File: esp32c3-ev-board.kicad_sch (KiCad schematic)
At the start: 33 parts, among them IC1 ESP32-C3, IC2 W25Q128JVSIQ, IC3 ACS711EEXTK-31AB-T, J1 Battery Neg(Series), J2 Battery Pos, SW1 SW_DPST_x2, Y1 40MHZ

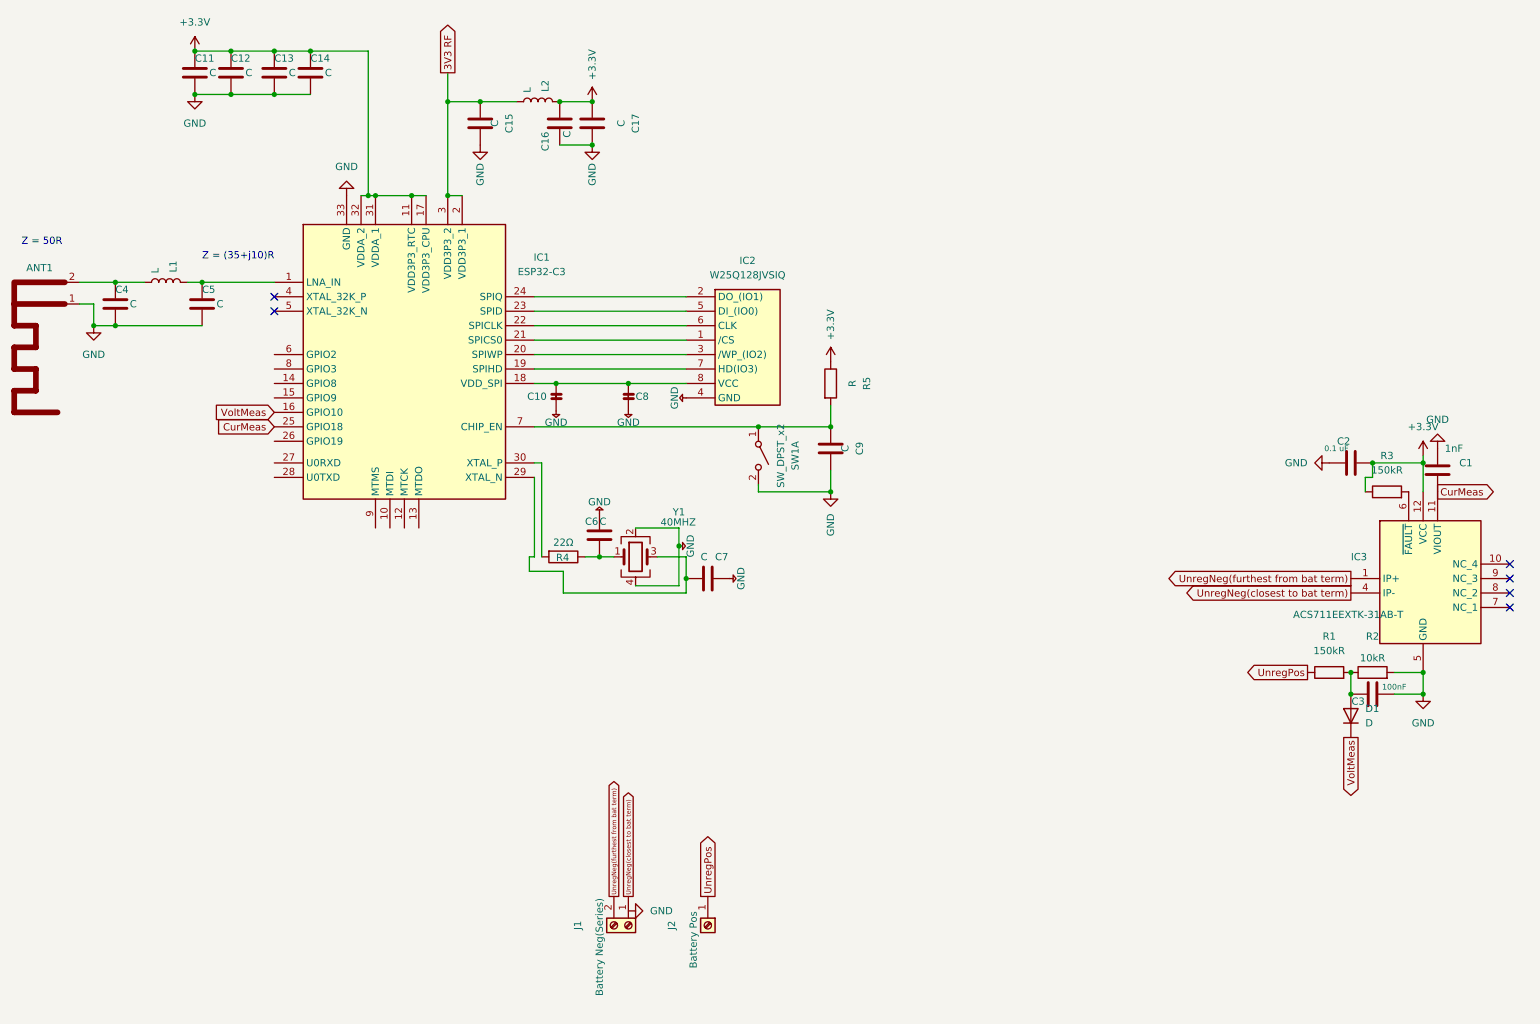
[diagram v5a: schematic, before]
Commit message: Tidy values and usb/esd prot
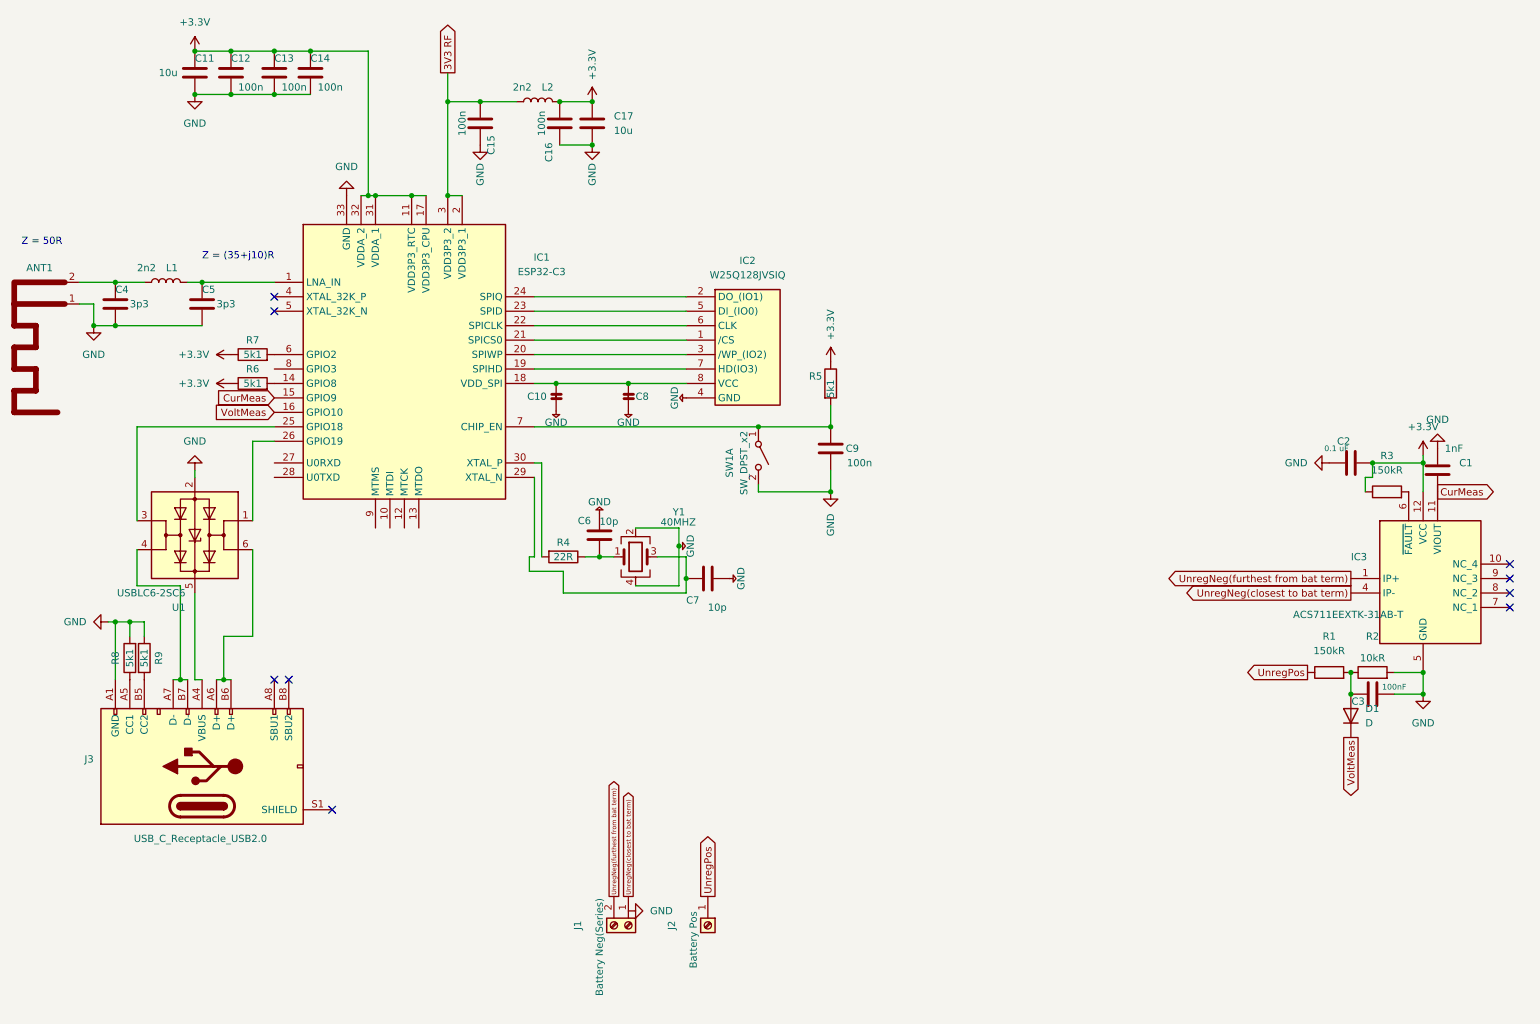
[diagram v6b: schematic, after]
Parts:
- added J3: USB_C_Receptacle_USB2.0, symbol Connector:USB_C_Receptacle_USB2.0
- added R6, R7, R8, R9: 5k1, symbol Device:R
- added U1: USBLC6-2SC6, Package_TO_SOT_SMD:SOT-23-6, symbol Power_Protection:USBLC6-2SC6
- C11, C17: value C -> 10u
- C12, C13, C14, C15, C16, C9: value C -> 100n
- C4, C5: value C -> 3p3
- C6, C7: value C -> 10p
- L1, L2: value L -> 2n2
- R4: value 22Ω -> 22R
- R5: value R -> 5k1
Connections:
- net +3.3V: now also R6.1, R7.1
- net CurMeas: now also IC1.15 (GPIO9); no longer IC1.25 (GPIO18)
- net GND: now also J3.A1 (GND), J3.A9 (VBUS), J3.B4 (VBUS), J3.B9 (VBUS), R8.2, R9.1, U1.2 (GND)
- net at IC1.14 (GPIO8): now also R6.2
- net at IC1.26 (GPIO19): now also U1.1 (I/O1)
- net at IC1.6 (GPIO2): now also R7.2
- new net: IC1.25 (GPIO18), U1.3 (I/O2)
- new net: J3.A7 (D-), J3.B7 (D-), U1.4 (I/O2)
- new net: J3.A4 (VBUS), U1.5 (VBUS)
- new net: J3.A6 (D+), J3.B6 (D+), U1.6 (I/O1)
- new net: J3.A5 (CC1), R8.1
- new net: J3.A12 (GND), J3.B1 (GND), J3.B12 (GND)
- new net: J3.B5 (CC2), R9.2
- no-connect marks 6 -> 9

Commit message: working on voltage and voltage mux
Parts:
- added C18: 100u, symbol Device:C_Polarized
- added C19: 1000u, symbol Device:C_Polarized
- added D2: MBR360, DIOAD2860W130L840D505, symbol MBR360:MBR360
- added L3: L, symbol Device:L
- added U2: LM2576HVS-3.3, Package_TO_SOT_SMD:TO-263-5_TabPin3, symbol Regulator_Switching:LM2576HVS-3.3
- IC1: value ESP32-C3 -> ESP32-C3FH4
- R1: value 150kR -> 180kR
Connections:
- net UnregNeg(closest to bat term) is gone; now on net GND: IC3.4 (IP-), J1.1 (Pin_1)
- net +3.3V: now also C19.1, L3.2, U2.4 (FB)
- net GND: now also C18.2, C19.2, D2.2 (A), U2.3 (GND), U2.5 (~{ON}/OFF)
- net UnregPos: now also C18.1, U2.1 (VIN)
- net VBUS: now reaches J3.A4 (VBUS), U1.5 (VBUS)
- new net: D2.1 (K), L3.1, U2.2 (OUT)
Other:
- note added: "If using external flash, use espfuse to burn EFUSE."
- note added: "MAX 60V"
- note added: "MAX 62.7V"
- moved on the sheet: U1

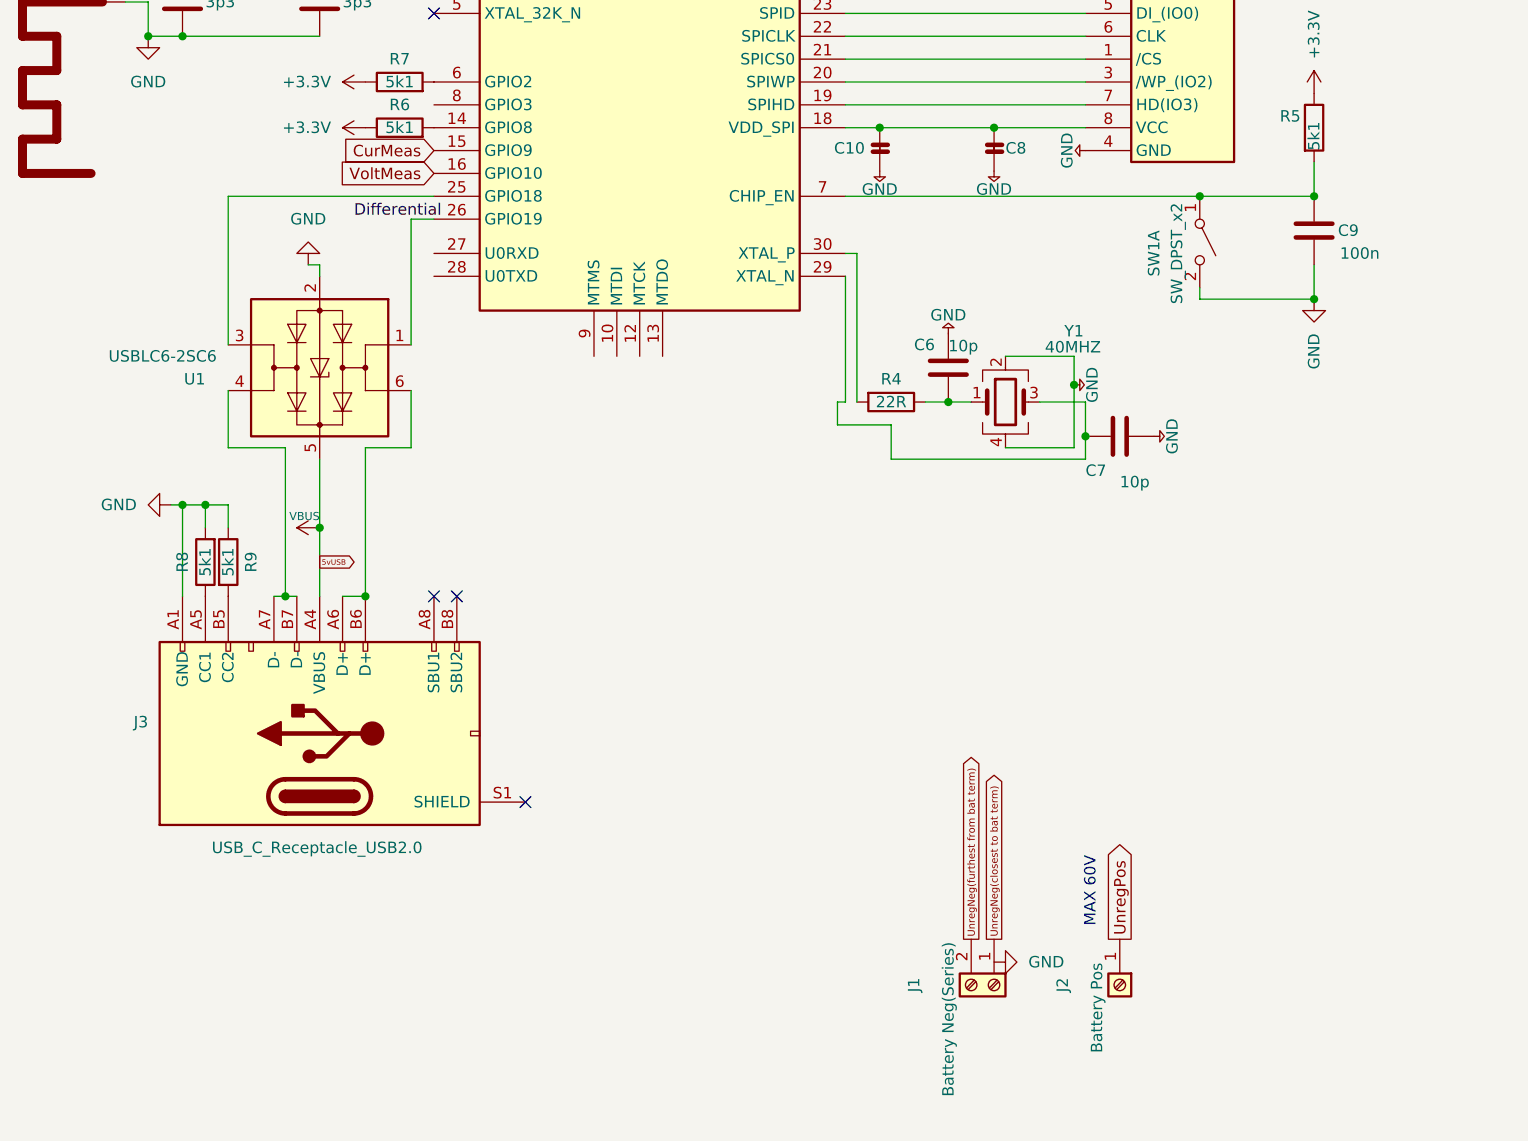
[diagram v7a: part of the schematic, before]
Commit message: Added Power supply diodes
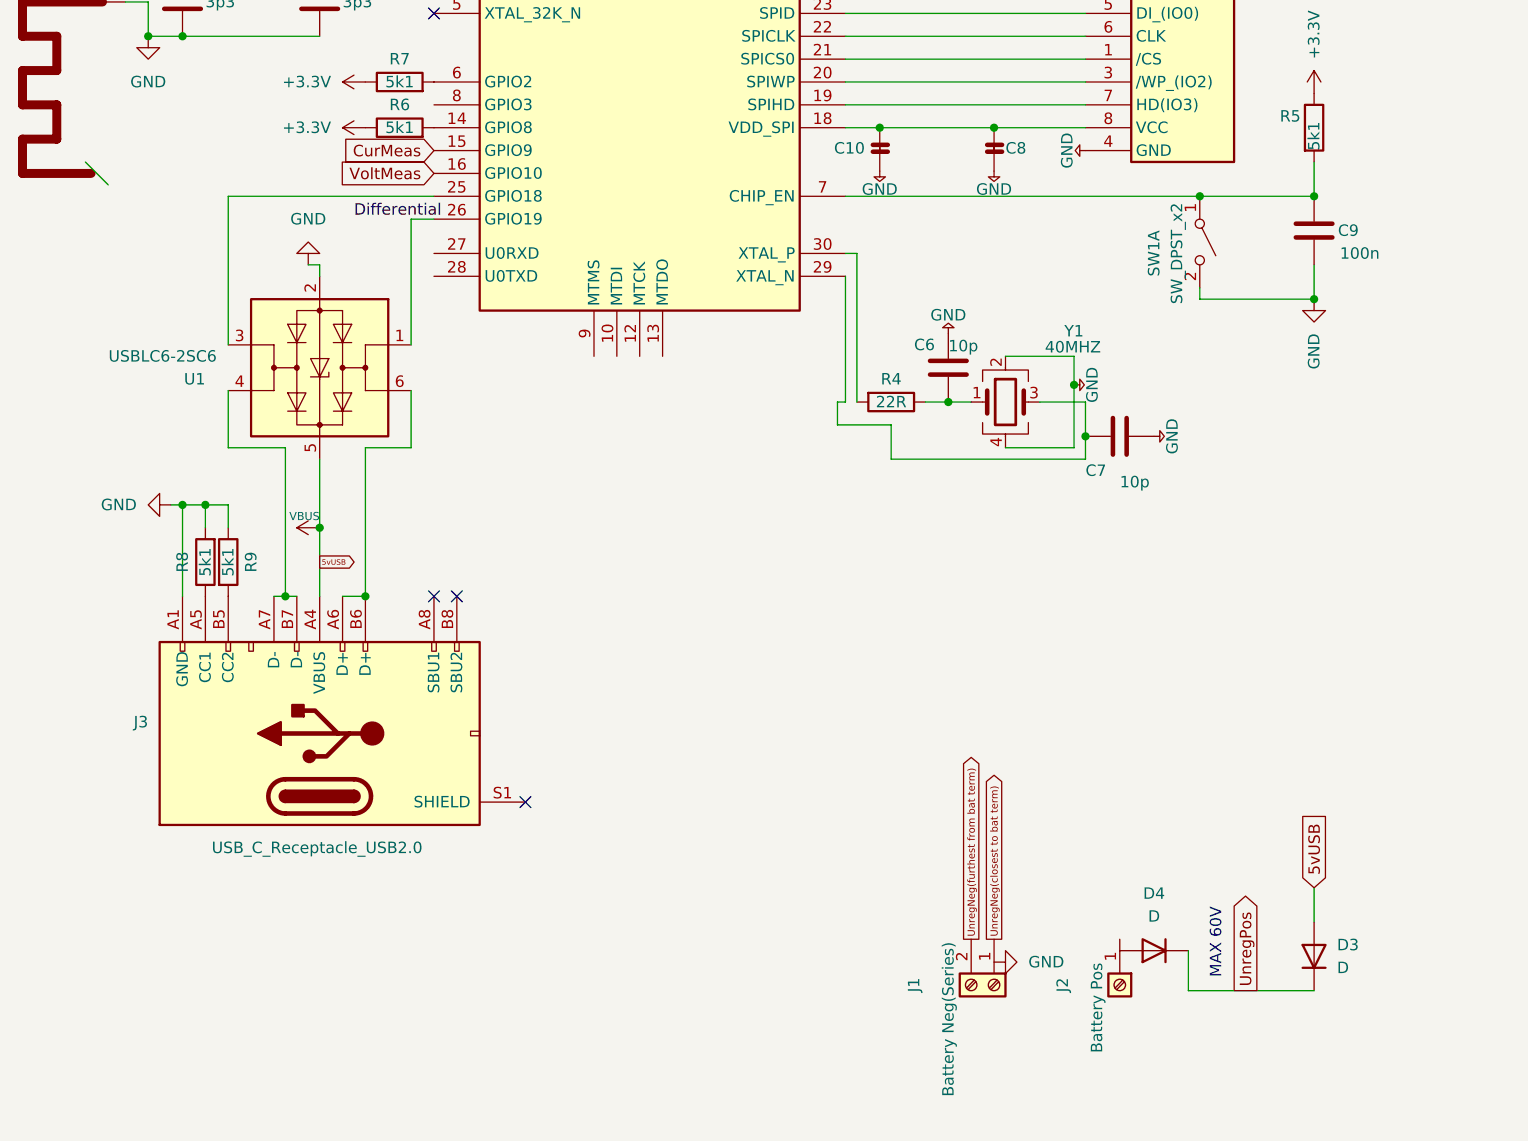
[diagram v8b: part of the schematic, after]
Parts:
- added D3, D4: D, symbol Device:D
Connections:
- net UnregPos: now also D3.1 (K), D4.1 (K); no longer J2.1 (Pin_1)
- net VBUS: now also D3.2 (A)
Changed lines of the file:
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@@
   (no_connect (at 60.96 72.39))
   (no_connect (at 278.13 119.38))
+  (bus_entry (at 22.225 91.44) (size 2.54 2.54)
+    (stroke (width 0) (type default))
+  )
   (wire (pts (xy 270.51 34.29) (xy 270.51 36.83))
     (stroke (width 0) (type default))
@@
     (stroke (width 0) (type default))
   )
+  (wire (pts (xy 144.78 179.07) (xy 144.78 183.515))
+    (stroke (width 0) (type default))
+  )
   (wire (pts (xy 35.56 132.08) (xy 35.56 129.54))
     (stroke (width 0) (type default))
@@
     (stroke (width 0) (type default))
   )
+  (wire (pts (xy 158.75 172.085) (xy 158.75 175.895))
+    (stroke (width 0) (type default))
+  )
   (wire (pts (xy 133.35 121.92) (xy 133.35 124.46))
     (stroke (width 0) (type default))
@@
     (stroke (width 0) (type default))
   )
+  (wire (pts (xy 144.78 183.515) (xy 158.75 183.515))
+    (stroke (width 0) (type default))
+  )
   (wire (pts (xy 123.19 87.63) (xy 133.35 87.63))
     (stroke (width 0) (type default))
@@
     (stroke (width 0) (type default))
   )
-  (text "MAX 60V" (at 134.62 176.53 90)
+  (text "MAX 60V" (at 148.59 182.245 90)
     (effects (font (size 1.27 1.27)) (justify left bottom))
   )
@@
     )
   )
+  (global_label "UnregPos" (shape output) (at 151.13 183.515 90) (fields_autoplaced)
+    (effects (font (size 1.27 1.27)) (justify left))
+    (property "Intersheetrefs" "${INTERSHEET_REFS}" (at 151.13 171.5794 90)
+      (effects (font (size 1.27 1.27)) (justify left) hide)
+    )
+  )
   (global_label "UnregPos" (shape output) (at 222.25 34.29 180) (fields_autoplaced)
     (effects (font (size 1.27 1.27)) (justify right))
@@
     )
   )
-  (global_label "UnregPos" (shape output) (at 137.16 177.8 90) (fields_autoplaced)
-    (effects (font (size 1.27 1.27)) (justify left))
-    (property "Intersheetrefs" "${INTERSHEET_REFS}" (at 137.16 165.8644 90)
-      (effects (font (size 1.27 1.27)) (justify left) hide)
-    )
-  )
   (global_label "CurMeas" (shape input) (at 60.96 90.17 180) (fields_autoplaced)
     (effects (font (size 1.27 1.27)) (justify right))
@@
     (property "Intersheetrefs" "${INTERSHEET_REFS}" (at 189.6317 55.88 0)
       (effects (font (size 1.27 1.27)) (justify right) hide)
+    )
+  )
+  (global_label "5vUSB" (shape input) (at 158.75 172.085 90) (fields_autoplaced)
+    (effects (font (size 1.27 1.27)) (justify left))
+    (property "Intersheetrefs" "${INTERSHEET_REFS}" (at 158.75 163.1921 90)
+      (effects (font (size 1.27 1.27)) (justify left) hide)
     )
   )
@@
     )
   )
+  (symbol (lib_id "Device:D") (at 140.97 179.07 180) (unit 1)
+    (in_bom yes) (on_board yes) (dnp no) (fields_autoplaced)
+    (property "Reference" "D4" (at 140.97 172.72 0)
+      (effects (font (size 1.27 1.27)))
+    )
+    (property "Value" "D" (at 140.97 175.26 0)
+      (effects (font (size 1.27 1.27)))
+    )
+    (property "Footprint" "" (at 140.97 179.07 0)
+      (effects (font (size 1.27 1.27)) hide)
+    )
+    (property "Datasheet" "~" (at 140.97 179.07 0)
+      (effects (font (size 1.27 1.27)) hide)
+    )
+    (property "Sim.Device" "D" (at 140.97 179.07 0)
+      (effects (font (size 1.27 1.27)) hide)
+    )
+    (property "Sim.Pins" "1=K 2=A" (at 140.97 179.07 0)
+      (effects (font (size 1.27 1.27)) hide)
+    )
+    (pin "1")
+    (pin "2")
+    (instances
+      (project "esp32c3-ev-board"
+        (path "/f5da1fcc-93b5-4c63-bb34-c18c11bc243c"
+          (reference "D4") (unit 1)
+        )
+      )
+    )
+  )
   (symbol (lib_id "Device:R") (at 256.54 106.68 90) (unit 1)
     (in_bom yes) (on_board yes) (dnp no) (fields_autoplaced)
@@
         )
       )
+    )
+  )
+  (symbol (lib_id "Device:D") (at 158.75 179.705 90) (unit 1)
+    (in_bom yes) (on_board yes) (dnp no) (fields_autoplaced)
+    (property "Reference" "D3" (at 161.29 178.435 90)
+      (effects (font (size 1.27 1.27)) (justify right))
+    )
+    (property "Value" "D" (at 161.29 180.975 90)
+      (effects (font (size 1.27 1.27)) (justify right))
+    )
+    (property "Footprint" "" (at 158.75 179.705 0)
+      (effects (font (size 1.27 1.27)) hide)
+    )
+    (property "Datasheet" "~" (at 158.75 179.705 0)
+      (effects (font (size 1.27 1.27)) hide)
+    )
+    (property "Sim.Device" "D" (at 158.75 179.705 0)
+      (effects (font (size 1.27 1.27)) hide)
+    )
+    (property "Sim.Pins" "1=K 2=A" (at 158.75 179.705 0)
+      (effects (font (size 1.27 1.27)) hide)
+    )
+    (pin "1")
+    (pin "2")
+    (instances
+      (project "esp32c3-ev-board"
+        (path "/f5da1fcc-93b5-4c63-bb34-c18c11bc243c"
+          (reference "D3") (unit 1)
+        )
+      )
